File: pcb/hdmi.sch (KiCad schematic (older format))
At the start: 11 parts, among them U7 TPD12S016PWR, X6 HDMI_A

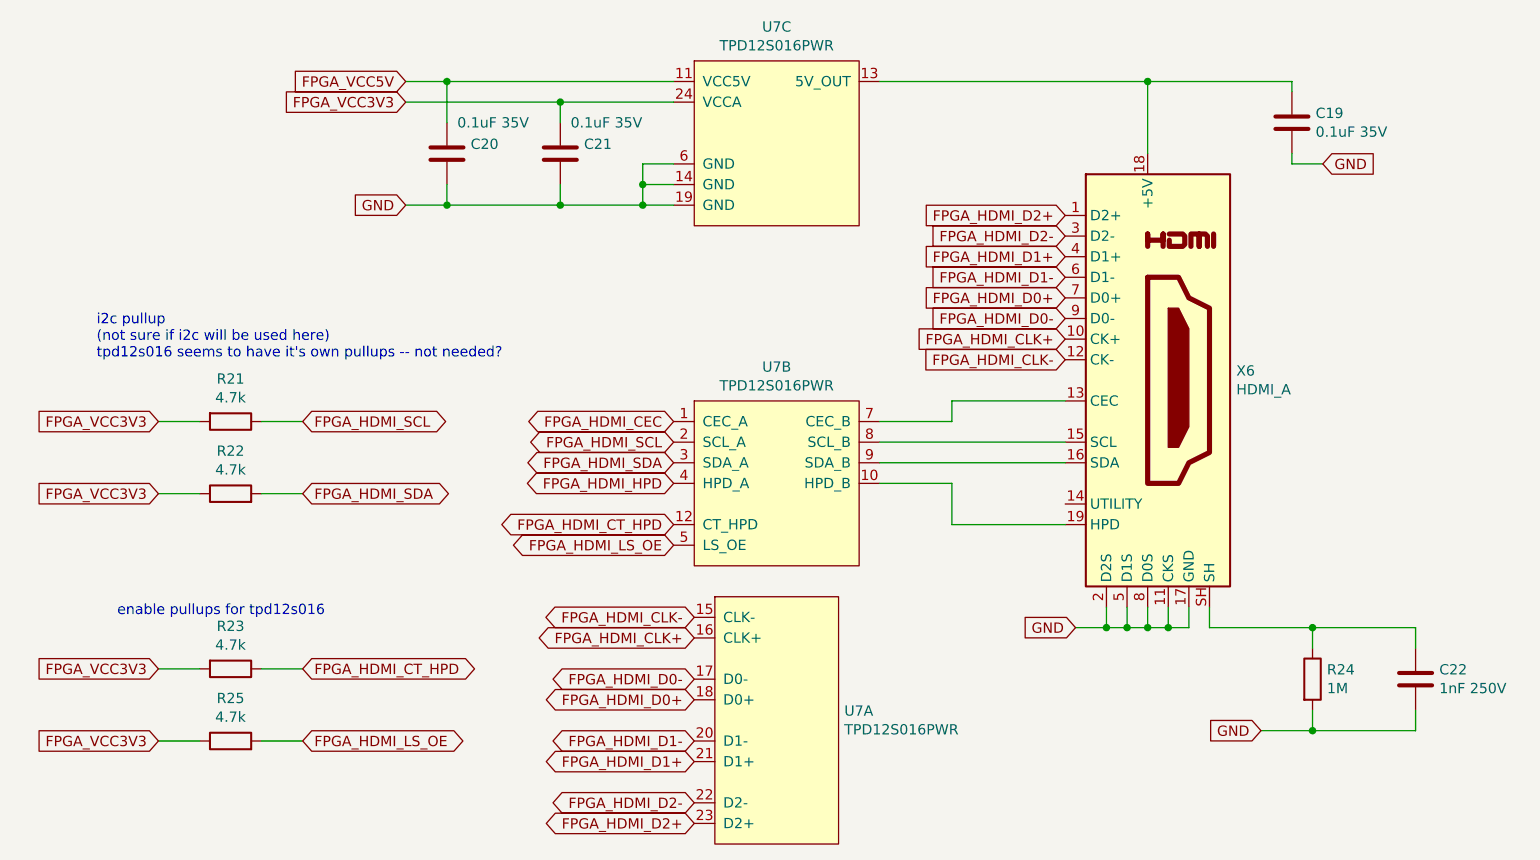
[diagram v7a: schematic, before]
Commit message: Buffers power scheme rework in progress, re-annotate board
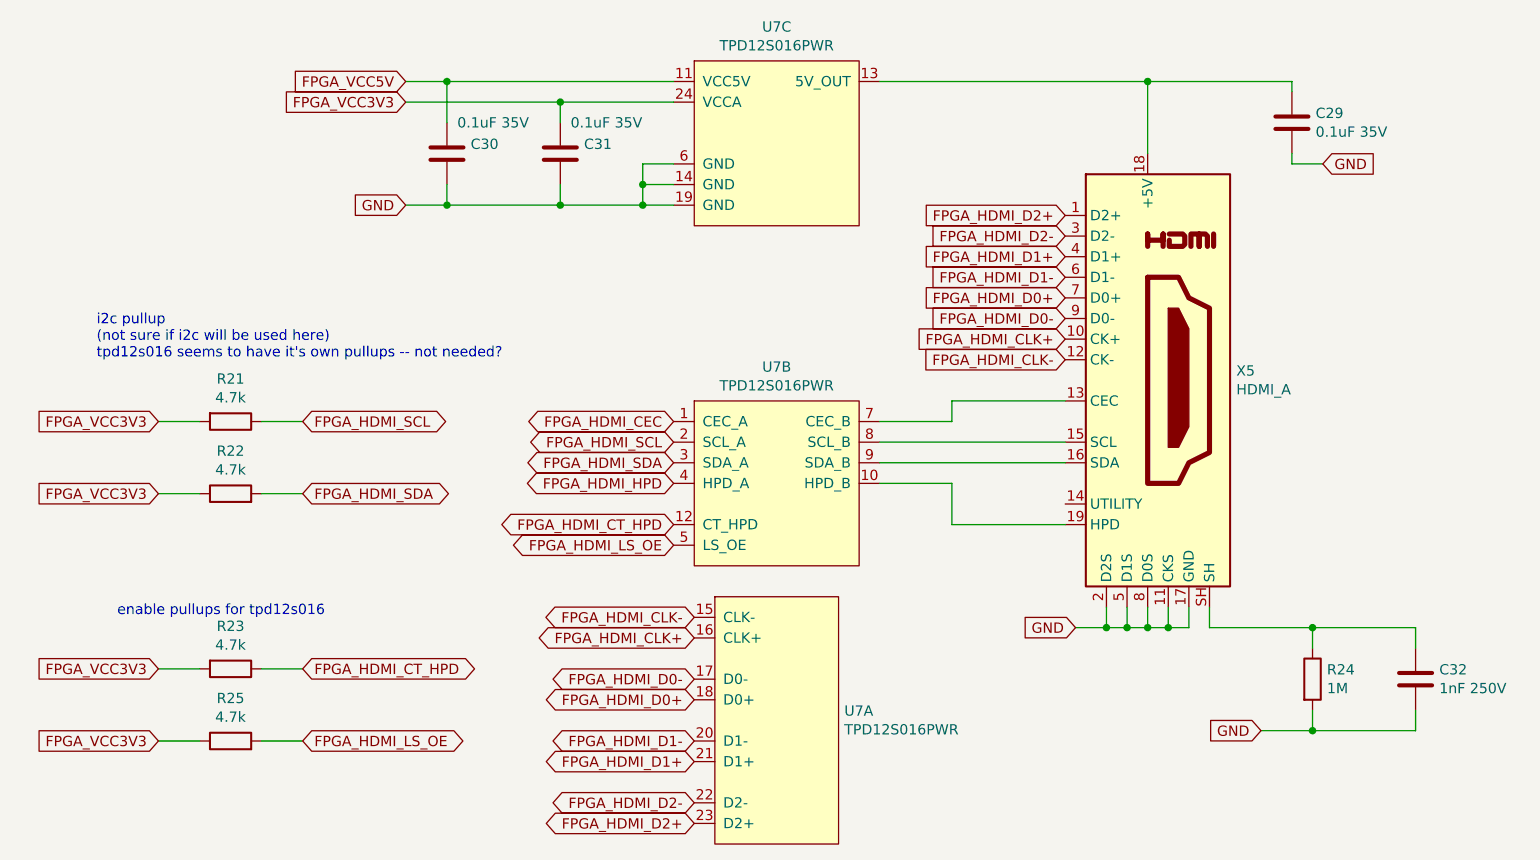
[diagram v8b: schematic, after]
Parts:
- renumbered C19 to C29, C20 to C30, C21 to C31, C22 to C32, X6 to X5
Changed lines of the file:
@@
 FPGA_HDMI_CLK-
 $Comp
-L Connector:HDMI_A X6
+L Connector:HDMI_A X5
 U 1 1 5E5A1311
 P 6300 2250
-F 0 "X6" H 6730 2296 50  0000 L CNN
+F 0 "X5" H 6730 2296 50  0000 L CNN
 F 1 "HDMI_A" H 6730 2205 50  0000 L CNN
 F 2 "WM1200:HDMI-19-02F" H 6325 2250 50  0001 C CNN
@@
 $EndComp
 $Comp
-L Device:C C22
+L Device:C C32
 U 1 1 5E5DF93C
 P 7600 3700
-F 0 "C22" H 7715 3746 50  0000 L CNN
+F 0 "C32" H 7715 3746 50  0000 L CNN
 F 1 "1nF 250V" H 7715 3655 50  0000 L CNN
 F 2 "Capacitor_SMD:C_0603_1608Metric_Pad1.05x0.95mm_HandSolder" H 7638 3550 50  0001 C CNN
@@
 FPGA_VCC3V3
 $Comp
-L Device:C C21
+L Device:C C31
 U 1 1 5E5EFF65
 P 3450 1150
-F 0 "C21" H 3565 1196 50  0000 L CNN
+F 0 "C31" H 3565 1196 50  0000 L CNN
 F 1 "0.1uF 35V" H 3500 1300 50  0000 L CNN
 F 2 "Capacitor_SMD:C_0603_1608Metric_Pad1.05x0.95mm_HandSolder" H 3488 1000 50  0001 C CNN
@@
 $EndComp
 $Comp
-L Device:C C20
+L Device:C C30
 U 1 1 5E5F9337
 P 2900 1150
-F 0 "C20" H 3015 1196 50  0000 L CNN
+F 0 "C30" H 3015 1196 50  0000 L CNN
 F 1 "0.1uF 35V" H 2950 1300 50  0000 L CNN
 F 2 "Capacitor_SMD:C_0603_1608Metric_Pad1.05x0.95mm_HandSolder" H 2938 1000 50  0001 C CNN
@@
 Connection ~ 3850 1400
 $Comp
-L Device:C C19
+L Device:C C29
 U 1 1 5E6181E4
 P 7000 1000
-F 0 "C19" H 7115 1046 50  0000 L CNN
+F 0 "C29" H 7115 1046 50  0000 L CNN
 F 1 "0.1uF 35V" H 7115 955 50  0000 L CNN
 F 2 "Capacitor_SMD:C_0603_1608Metric_Pad1.05x0.95mm_HandSolder" H 7038 850 50  0001 C CNN
